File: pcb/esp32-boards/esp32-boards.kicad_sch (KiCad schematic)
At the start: 41 parts, among them J1 BOOT_MODE, J2 USB_B_Micro, J3 BATTERY, Q1 Q_Photo_NPN, SW1 RESET, SW2 BAT_EN, U1 ESP32-C3-WROOM-02, U2 MAX40200AUK, U3 MCP73831-2-OT, U4 LD39150DT33

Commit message: rename reporter to a generic name
The same PCB can be used for the reporter and controller. They are
essentially the same, except the controller will have a few more
components. These components can be no-loaded for the reporter.
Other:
- title: laser photogate reporter -> laser photogate ESP32 board

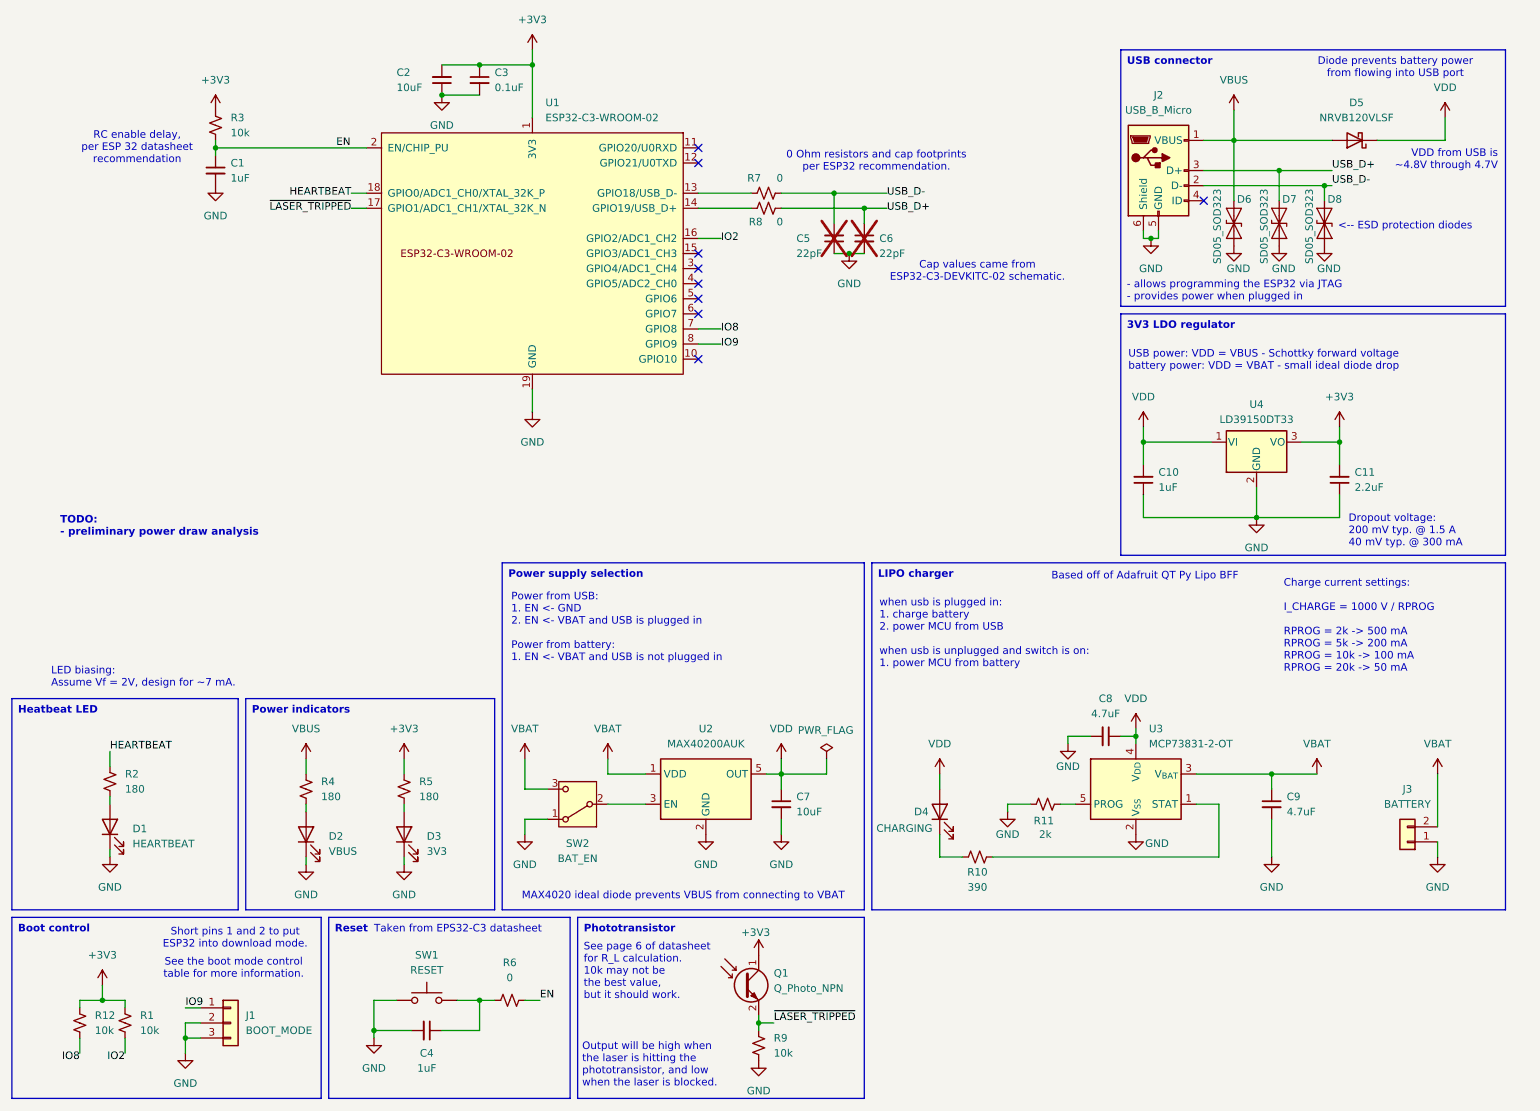
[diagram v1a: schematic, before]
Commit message: add LCD and start button
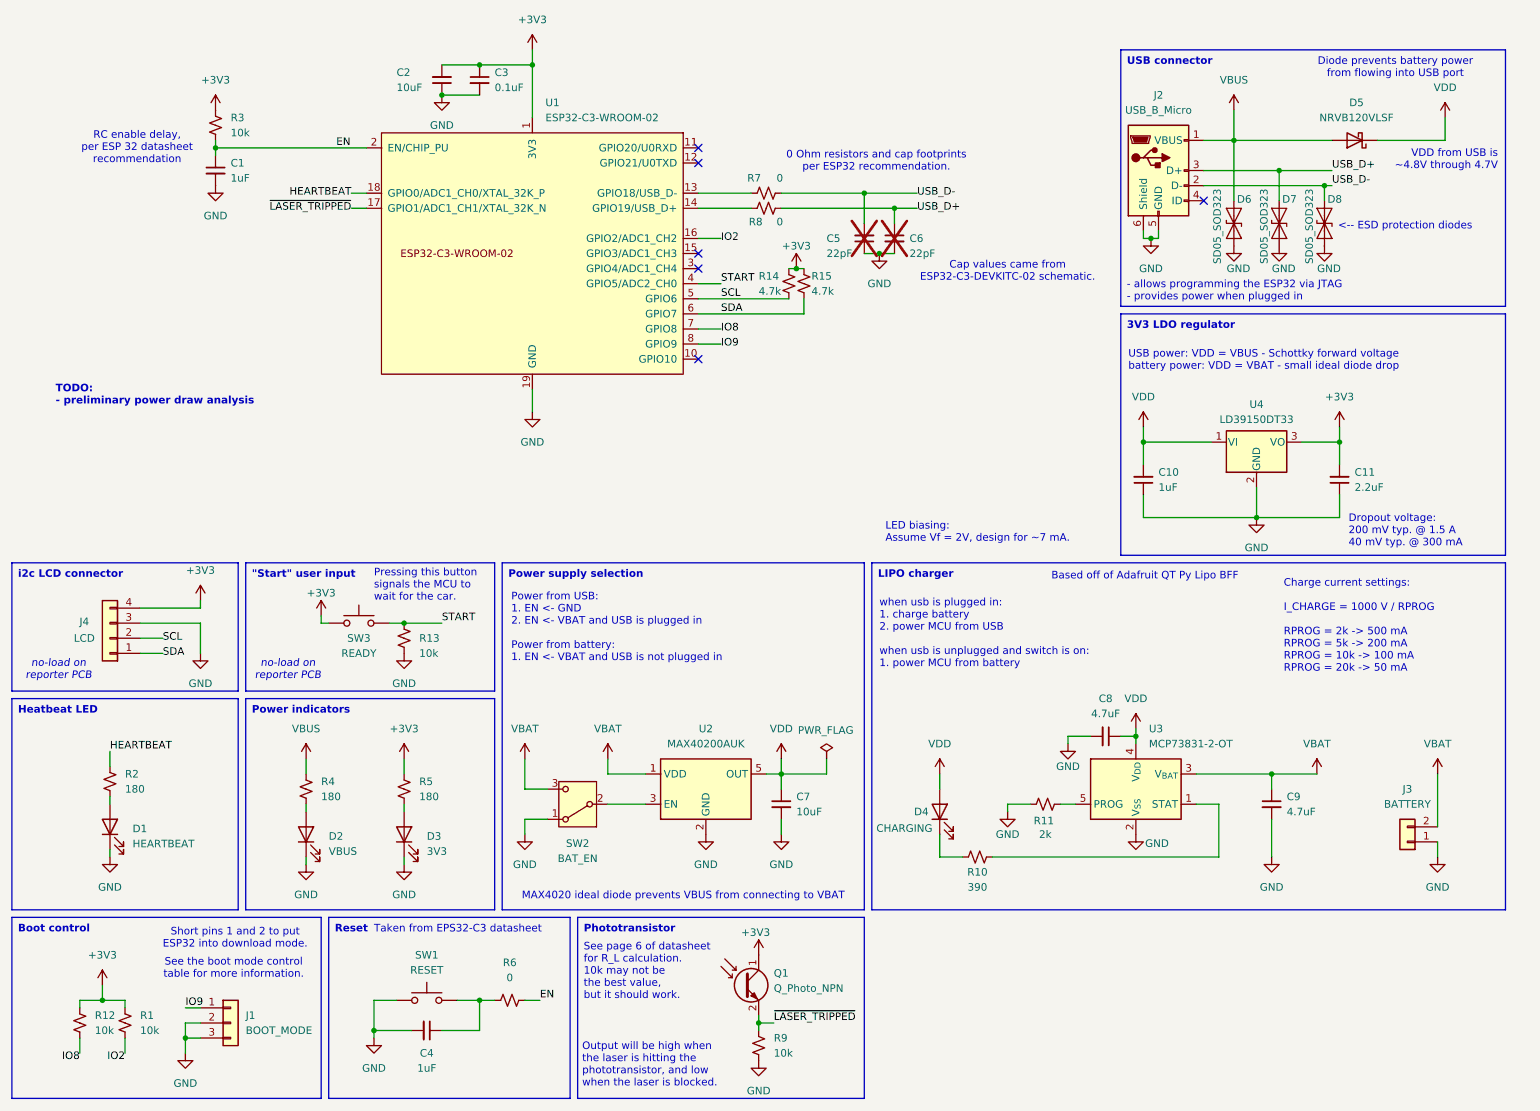
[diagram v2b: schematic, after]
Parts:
- added J4: LCD, Connector_JST:JST_PH_B4B-PH-K_1x04_P2.00mm_Vertical, symbol Connector_Generic:Conn_01x04
- added R13: 10k, Resistor_SMD:R_1206_3216Metric_Pad1.30x1.75mm_HandSolder, symbol Device:R_Small_US
- added R14, R15: 4.7k, Resistor_SMD:R_1206_3216Metric_Pad1.30x1.75mm_HandSolder, symbol Device:R_Small_US
- added SW3: READY, Connector_JST:JST_PH_B2B-PH-K_1x02_P2.00mm_Vertical, symbol Switch:SW_Push
- J3: Part Number B2B-XH-A -> B2B-PH-K-S
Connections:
- net +3V3: now also J4.4 (Pin_4), R14.1, R15.1, SW3.1
- net GND: now also J4.3 (Pin_3), R13.2
- net START: now reaches U1.4 (GPIO5/ADC2_CH0)
- net START: now also R13.1, SW3.2
- net SCL: now reaches U1.5 (GPIO6)
- net SCL: now also J4.2 (Pin_2), R14.2
- net SDA: now reaches U1.6 (GPIO7)
- net SDA: now also J4.1 (Pin_1), R15.2
- no-connect marks 9 -> 6
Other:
- note added: "Pressing this button signals the MCU to wait for the car."
- note added: "no-load on reporter PCB"
- moved on the sheet: C5, C6

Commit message: switch to 0805 for most components
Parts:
- C1, C10, C11, C2, C3, C4, C5, C6, C7, C8, C9: footprint Capacitor_SMD:C_1206_3216Metric_Pad1.33x1.80mm_HandSolder -> Capacitor_SMD:C_0805_2012Metric_Pad1.18x1.45mm_HandSolder
- R1, R10, R11, R12, R13, R14, R15, R2, R3, R4, R5, R6, R7, R8, R9: footprint Resistor_SMD:R_1206_3216Metric_Pad1.30x1.75mm_HandSolder -> Resistor_SMD:R_0805_2012Metric_Pad1.20x1.40mm_HandSolder
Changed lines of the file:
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@@
 			)
 		)
-		(property "Footprint" "Capacitor_SMD:C_1206_3216Metric_Pad1.33x1.80mm_HandSolder"
+		(property "Footprint" "Capacitor_SMD:C_0805_2012Metric_Pad1.18x1.45mm_HandSolder"
 			(at 162.56 57.15 0)
 			(effects
@@
 			)
 		)
-		(property "Footprint" "Resistor_SMD:R_1206_3216Metric_Pad1.30x1.75mm_HandSolder"
+		(property "Footprint" "Resistor_SMD:R_0805_2012Metric_Pad1.20x1.40mm_HandSolder"
 			(at 176.53 161.29 0)
 			(effects
@@
 			)
 		)
-		(property "Footprint" "Resistor_SMD:R_1206_3216Metric_Pad1.30x1.75mm_HandSolder"
+		(property "Footprint" "Resistor_SMD:R_0805_2012Metric_Pad1.20x1.40mm_HandSolder"
 			(at 80.01 124.46 0)
 			(effects
@@
 			)
 		)
-		(property "Footprint" "Capacitor_SMD:C_1206_3216Metric_Pad1.33x1.80mm_HandSolder"
+		(property "Footprint" "Capacitor_SMD:C_0805_2012Metric_Pad1.18x1.45mm_HandSolder"
 			(at 83.82 190.5 0)
 			(effects
@@
 			)
 		)
-		(property "Footprint" "Resistor_SMD:R_1206_3216Metric_Pad1.30x1.75mm_HandSolder"
+		(property "Footprint" "Resistor_SMD:R_0805_2012Metric_Pad1.20x1.40mm_HandSolder"
 			(at 48.26 38.1 0)
 			(effects
@@
 			)
 		)
-		(property "Footprint" "Resistor_SMD:R_1206_3216Metric_Pad1.30x1.75mm_HandSolder"
+		(property "Footprint" "Resistor_SMD:R_0805_2012Metric_Pad1.20x1.40mm_HandSolder"
 			(at 187.96 152.4 0)
 			(effects
@@
 			)
 		)
-		(property "Footprint" "Resistor_SMD:R_1206_3216Metric_Pad1.30x1.75mm_HandSolder"
+		(property "Footprint" "Resistor_SMD:R_0805_2012Metric_Pad1.20x1.40mm_HandSolder"
 			(at 140.97 49.53 0)
 			(effects
@@
 			)
 		)
-		(property "Footprint" "Capacitor_SMD:C_1206_3216Metric_Pad1.33x1.80mm_HandSolder"
+		(property "Footprint" "Capacitor_SMD:C_0805_2012Metric_Pad1.18x1.45mm_HandSolder"
 			(at 204.47 97.79 0)
 			(effects
@@
 			)
 		)
-		(property "Footprint" "Capacitor_SMD:C_1206_3216Metric_Pad1.33x1.80mm_HandSolder"
+		(property "Footprint" "Capacitor_SMD:C_0805_2012Metric_Pad1.18x1.45mm_HandSolder"
 			(at 198.12 140.97 0)
 			(effects
@@
 			)
 		)
-		(property "Footprint" "Resistor_SMD:R_1206_3216Metric_Pad1.30x1.75mm_HandSolder"
+		(property "Footprint" "Resistor_SMD:R_0805_2012Metric_Pad1.20x1.40mm_HandSolder"
 			(at 80.01 149.86 0)
 			(effects
@@
 			)
 		)
-		(property "Footprint" "Resistor_SMD:R_1206_3216Metric_Pad1.30x1.75mm_HandSolder"
+		(property "Footprint" "Resistor_SMD:R_0805_2012Metric_Pad1.20x1.40mm_HandSolder"
 			(at 63.5 149.86 0)
 			(effects
@@
 			)
 		)
-		(property "Footprint" "Capacitor_SMD:C_1206_3216Metric_Pad1.33x1.80mm_HandSolder"
+		(property "Footprint" "Capacitor_SMD:C_0805_2012Metric_Pad1.18x1.45mm_HandSolder"
 			(at 237.49 97.79 0)
 			(effects
@@
 			)
 		)
-		(property "Footprint" "Resistor_SMD:R_1206_3216Metric_Pad1.30x1.75mm_HandSolder"
+		(property "Footprint" "Resistor_SMD:R_0805_2012Metric_Pad1.20x1.40mm_HandSolder"
 			(at 33.02 189.23 0)
 			(effects
@@
 			)
 		)
-		(property "Footprint" "Capacitor_SMD:C_1206_3216Metric_Pad1.33x1.80mm_HandSolder"
+		(property "Footprint" "Capacitor_SMD:C_0805_2012Metric_Pad1.18x1.45mm_HandSolder"
 			(at 48.26 45.72 0)
 			(effects
@@
 			)
 		)
-		(property "Footprint" "Capacitor_SMD:C_1206_3216Metric_Pad1.33x1.80mm_HandSolder"
+		(property "Footprint" "Capacitor_SMD:C_0805_2012Metric_Pad1.18x1.45mm_HandSolder"
 			(at 92.71 30.48 0)
 			(effects
@@
 			)
 		)
-		(property "Footprint" "Resistor_SMD:R_1206_3216Metric_Pad1.30x1.75mm_HandSolder"
+		(property "Footprint" "Resistor_SMD:R_0805_2012Metric_Pad1.20x1.40mm_HandSolder"
 			(at 147.32 64.77 0)
 			(effects
@@
 			)
 		)
-		(property "Footprint" "Resistor_SMD:R_1206_3216Metric_Pad1.30x1.75mm_HandSolder"
+		(property "Footprint" "Resistor_SMD:R_0805_2012Metric_Pad1.20x1.40mm_HandSolder"
 			(at 97.79 185.42 0)
 			(effects
@@
 			)
 		)
-		(property "Footprint" "Resistor_SMD:R_1206_3216Metric_Pad1.30x1.75mm_HandSolder"
+		(property "Footprint" "Resistor_SMD:R_0805_2012Metric_Pad1.20x1.40mm_HandSolder"
 			(at 139.7 193.04 0)
 			(effects
@@
 			)
 		)
-		(property "Footprint" "Resistor_SMD:R_1206_3216Metric_Pad1.30x1.75mm_HandSolder"
+		(property "Footprint" "Resistor_SMD:R_0805_2012Metric_Pad1.20x1.40mm_HandSolder"
 			(at 30.48 148.59 0)
 			(effects
@@
 			)
 		)
-		(property "Footprint" "Capacitor_SMD:C_1206_3216Metric_Pad1.33x1.80mm_HandSolder"
+		(property "Footprint" "Capacitor_SMD:C_0805_2012Metric_Pad1.18x1.45mm_HandSolder"
 			(at 86.36 30.48 0)
 			(effects
@@
 			)
 		)
-		(property "Footprint" "Resistor_SMD:R_1206_3216Metric_Pad1.30x1.75mm_HandSolder"
+		(property "Footprint" "Resistor_SMD:R_0805_2012Metric_Pad1.20x1.40mm_HandSolder"
 			(at 25.4 189.23 0)
 			(effects
@@
 			)
 		)
-		(property "Footprint" "Capacitor_SMD:C_1206_3216Metric_Pad1.33x1.80mm_HandSolder"
+		(property "Footprint" "Capacitor_SMD:C_0805_2012Metric_Pad1.18x1.45mm_HandSolder"
 			(at 157.48 57.15 0)
 			(effects
@@
 			)
 		)
-		(property "Footprint" "Resistor_SMD:R_1206_3216Metric_Pad1.30x1.75mm_HandSolder"
+		(property "Footprint" "Resistor_SMD:R_0805_2012Metric_Pad1.20x1.40mm_HandSolder"
 			(at 144.78 64.77 0)
 			(effects
@@
 			)
 		)
-		(property "Footprint" "Resistor_SMD:R_1206_3216Metric_Pad1.30x1.75mm_HandSolder"
+		(property "Footprint" "Resistor_SMD:R_0805_2012Metric_Pad1.20x1.40mm_HandSolder"
 			(at 140.97 52.07 0)
 			(effects
@@
 			)
 		)
-		(property "Footprint" "Capacitor_SMD:C_1206_3216Metric_Pad1.33x1.80mm_HandSolder"
+		(property "Footprint" "Capacitor_SMD:C_0805_2012Metric_Pad1.18x1.45mm_HandSolder"
 			(at 143.51 152.4 0)
 			(effects
@@
 			)
 		)
-		(property "Footprint" "Capacitor_SMD:C_1206_3216Metric_Pad1.33x1.80mm_HandSolder"
+		(property "Footprint" "Capacitor_SMD:C_0805_2012Metric_Pad1.18x1.45mm_HandSolder"
 			(at 226.06 152.4 0)
 			(effects

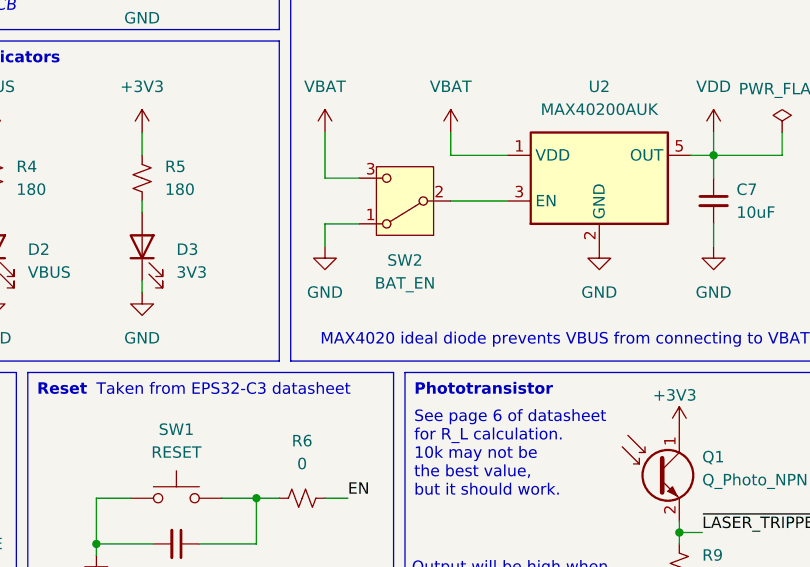
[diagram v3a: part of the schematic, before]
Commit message: update battery switch name
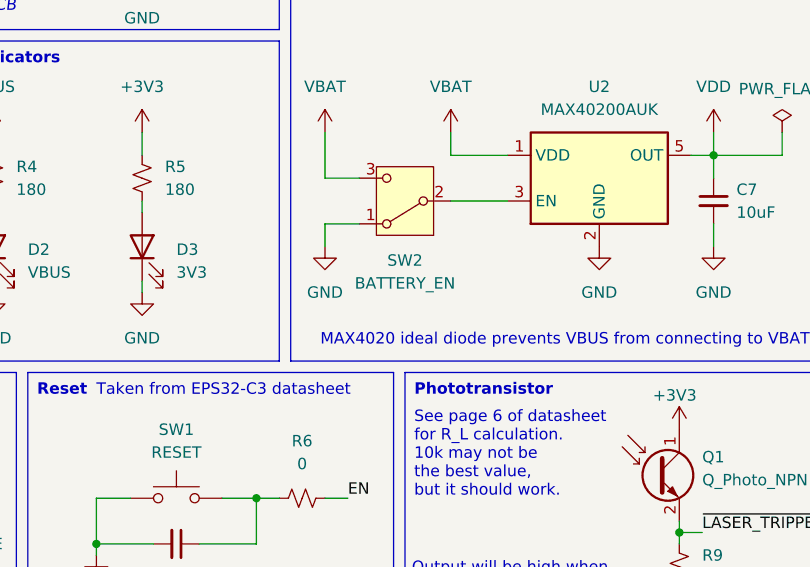
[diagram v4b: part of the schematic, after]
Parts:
- SW2: value BAT_EN -> BATTERY_EN
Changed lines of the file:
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@@
 			)
 		)
-		(property "Value" "BAT_EN"
+		(property "Value" "BATTERY_EN"
 			(at 109.22 161.544 0)
 			(effects

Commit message: finish first draft of layout
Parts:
- removed J1: BOOT_MODE, Connector_PinHeader_2.54mm:PinHeader_1x03_P2.54mm_Vertical, symbol Connector_Generic:Conn_01x03
- added C12: 0.1uF, Capacitor_SMD:C_0805_2012Metric_Pad1.18x1.45mm_HandSolder, symbol Device:C_Small
- added SW4: BOOT_MODE, Button_Switch_THT:SW_PUSH_6mm_H4.3mm, symbol Switch:SW_Push
- D1: value HEARTBEAT -> STATUS
- D4: value CHARGING -> CHARGE
- SW3: value READY -> START
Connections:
- net GND: now also C12.2, SW4.1
- net HEARTBEAT: now also U1.17 (GPIO1/ADC1_CH1/XTAL_32K_N); no longer U1.18 (GPIO0/ADC1_CH0/XTAL_32K_P)
- net IO9: now also SW4.2
- net VBAT: now also C12.1
- net ~{LASER_TRIPPED}: now also U1.18 (GPIO0/ADC1_CH0/XTAL_32K_P); no longer U1.17 (GPIO1/ADC1_CH1/XTAL_32K_N)
- net D+: now reaches R7.1, U1.13 (GPIO18/USB_D-)
- net D-: now reaches R8.1, U1.14 (GPIO19/USB_D+)
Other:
- moved on the sheet: SW2
